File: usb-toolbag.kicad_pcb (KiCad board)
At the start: 4 copper layers, 49.8 x 17.9 mm, 33 parts, among them J1 USB_A, J2 Conn_01x25_Pin, SW1 KMR2, SW2 KMR2, U1 29F32G08-TSOP48, U2 RT9080-3.3, U3 RP2040, U4 8MB QSPI, Y1 12MHz

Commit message: something something overworking myself...
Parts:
- moved C4 2.00 mm to (115.4, 106.3), turned to 0 degrees
- moved R6 0.93 mm to (120.8, 109.1)
- moved C5 0.73 mm to (115.8, 110.4), turned to 90 degrees
- moved R2 0.72 mm to (131.0, 115.5)
- moved R1 0.42 mm to (128.3, 115.9)
- moved C6 0.33 mm to (126.1, 115.9)
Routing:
- net Net-(U3-XOUT): track 9.29 -> 8.03 mm
- net /GPIO16: track 19.9 -> 21.0 mm
- net /GPIO17: track 21.3 -> 22.2 mm
- net Net-(U3-USB_DM): track 4.81 -> 4.06 mm
- net Net-(J1-D-): track 9.53 -> 10.2 mm

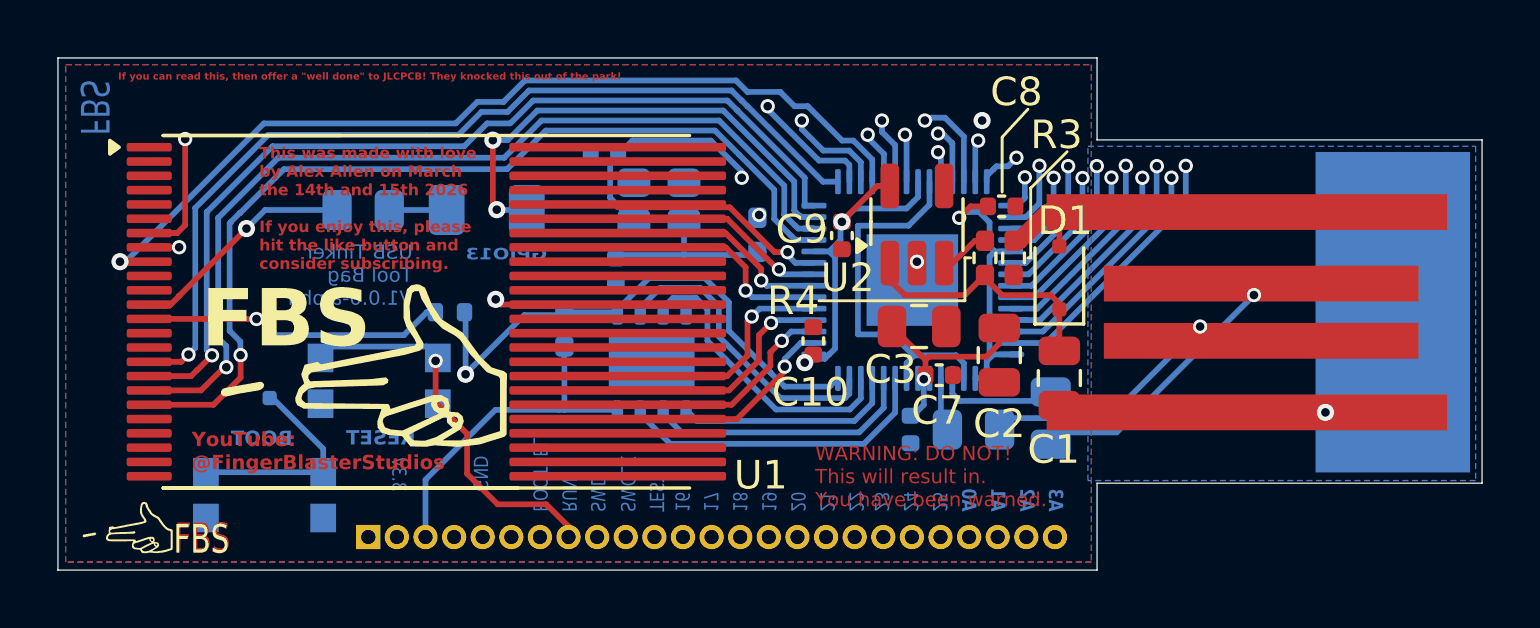
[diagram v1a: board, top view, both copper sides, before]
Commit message: made silk screen pretty
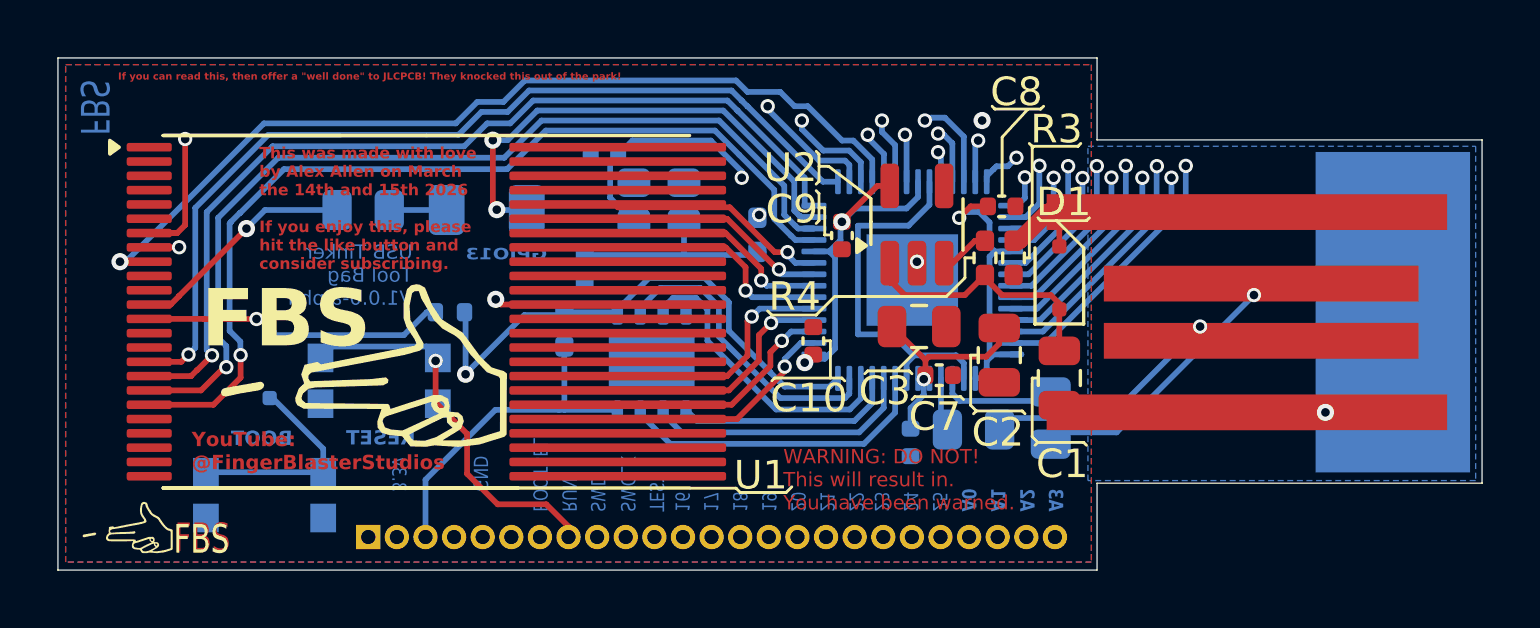
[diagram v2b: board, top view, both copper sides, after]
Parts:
- moved C5 1.09 mm to (114.8, 110.3)
- moved C6 0.45 mm to (126.1, 116.3)
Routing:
- net Net-(C5-Pad2): track 6.39 -> 7.43 mm
